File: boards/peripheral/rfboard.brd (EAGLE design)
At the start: 30 x 60 mm, 27 parts, among them Q1 IRLML5203, Q2 IRLML5203, Q3 IRLML5203, Q4 IRLML5203

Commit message: fixed improper ground issue
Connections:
- removed net N_GND: AMB2.2, C1.2, OPT101.3, OPT101.8
- net GND: now also AMB2.2, C1.2, OPT101.3, OPT101.8
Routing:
- removed copper zone on layer 16, net N_GND
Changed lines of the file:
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@@
 <via x="15.3162" y="55.2704" extent="1-16" drill="0.508" alwaysstop="yes"/>
 <wire x1="24.7904" y1="21.1582" x2="24.7904" y2="21.1836" width="0.6096" layer="16"/>
+<contactref element="AMB2" pad="2"/>
+<contactref element="C1" pad="2"/>
+<contactref element="OPT101" pad="8"/>
+<contactref element="OPT101" pad="3"/>
+<polygon width="0.6096" layer="16">
+<vertex x="30" y="19.5"/>
+<vertex x="30.1524" y="-0.1016"/>
+<vertex x="0.1524" y="-0.1016"/>
+<vertex x="0" y="19.5"/>
+</polygon>
 </signal>
 <signal name="AMB_OUT">
@@
 <wire x1="13.351" y1="26.7056" x2="13.351" y2="25.019" width="0.6096" layer="16"/>
 </signal>
-<signal name="N_GND" class="1">
-<contactref element="AMB2" pad="2"/>
-<contactref element="C1" pad="2"/>
-<contactref element="OPT101" pad="8"/>
-<contactref element="OPT101" pad="3"/>
-<polygon width="0.6096" layer="16">
-<vertex x="30" y="19.5"/>
-<vertex x="30.1524" y="-0.1016"/>
-<vertex x="0.1524" y="-0.1016"/>
-<vertex x="0" y="19.5"/>
-</polygon>
-</signal>
 <signal name="L4">

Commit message: Cleanup issues, working on powerboard res move
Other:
- board text added: "Xbee Forward"
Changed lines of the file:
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@@
 <?xml version="1.0" encoding="utf-8"?>
 <!DOCTYPE eagle SYSTEM "eagle.dtd">
-<eagle version="6.4">
+<eagle version="6.5.0">
 <drawing>
 <settings>
@@
 <setting verticaltext="up"/>
 </settings>
-<grid distance="1" unitdist="mil" unit="mil" style="lines" multiple="20" display="no" altdistance="0.025" altunitdist="inch" altunit="inch"/>
+<grid distance="0.02" unitdist="mm" unit="mm" style="lines" multiple="20" display="no" altdistance="0.025" altunitdist="inch" altunit="inch"/>
 <layers>
 <layer number="1" name="Top" color="4" fill="1" visible="yes" active="yes"/>
@@
 <text x="22.479" y="22.6314" size="0.8128" layer="25" rot="R90">AD4/DI4</text>
 <text x="2.7432" y="31.2928" size="0.8128" layer="25" rot="R90">8/6/13</text>
+<wire x1="24.0284" y1="42.799" x2="24.0284" y2="41.148" width="0.4064" layer="21"/>
+<wire x1="24.0284" y1="41.148" x2="27.178" y2="37.9984" width="0.4064" layer="21"/>
+<wire x1="27.178" y1="37.9984" x2="27.178" y2="26.2636" width="0.4064" layer="21"/>
+<wire x1="27.178" y1="26.2636" x2="23.7744" y2="22.86" width="0.4064" layer="21"/>
+<wire x1="23.7744" y1="22.86" x2="23.7744" y2="22.5044" width="0.4064" layer="21"/>
+<wire x1="23.7744" y1="22.5044" x2="23.6474" y2="22.3774" width="0.4064" layer="21"/>
+<text x="25.2222" y="37.1348" size="0.8128" layer="21" rot="R270">Xbee Forward</text>
+<wire x1="16.5862" y1="5.9436" x2="16.5354" y2="8.0264" width="0.4064" layer="21" curve="-180"/>
+<wire x1="16.5354" y1="8.0264" x2="16.5354" y2="9.779" width="0.4064" layer="21"/>
+<wire x1="16.5354" y1="5.8674" x2="16.5354" y2="4.064" width="0.4064" layer="21"/>
+<circle x="4" y="56" radius="3.668" width="0.4064" layer="21"/>
+<circle x="26" y="56" radius="3.668" width="0.4064" layer="21"/>
+<circle x="26" y="4" radius="3.668" width="0.4064" layer="21"/>
+<circle x="4" y="4" radius="3.668" width="0.4064" layer="21"/>
 </plain>
 <attributes>

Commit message: fixed PRF labels
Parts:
- AMB2: value 96k -> 200k
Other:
- board text added: "v.2013/09/26"
- board text removed: "8/6/13"
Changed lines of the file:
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@@
 <text x="20.3708" y="22.5298" size="0.8128" layer="25" rot="R90">CTS/DI7</text>
 <text x="22.479" y="22.6314" size="0.8128" layer="25" rot="R90">AD4/DI4</text>
-<text x="2.7432" y="31.2928" size="0.8128" layer="25" rot="R90">8/6/13</text>
+<text x="2.6832" y="28.7328" size="0.8128" layer="25" rot="R90">v.2013/09/26</text>
 <wire x1="24.0284" y1="42.799" x2="24.0284" y2="41.148" width="0.4064" layer="21"/>
 <wire x1="24.0284" y1="41.148" x2="27.178" y2="37.9984" width="0.4064" layer="21"/>
@@
 <attribute name="VALUE" x="1.1684" y="7.5438" size="0.8128" layer="28" rot="MR90"/>
 </element>
-<element name="AMB2" library="resistor" package="R0805" value="96k" x="21.1328" y="14.986" smashed="yes" rot="MR0">
+<element name="AMB2" library="resistor" package="R0805" value="200k" x="21.1328" y="14.986" smashed="yes" rot="MR0">
 <attribute name="VALUE" x="22.3012" y="16.0782" size="0.8128" layer="28" rot="MR0"/>
 </element>

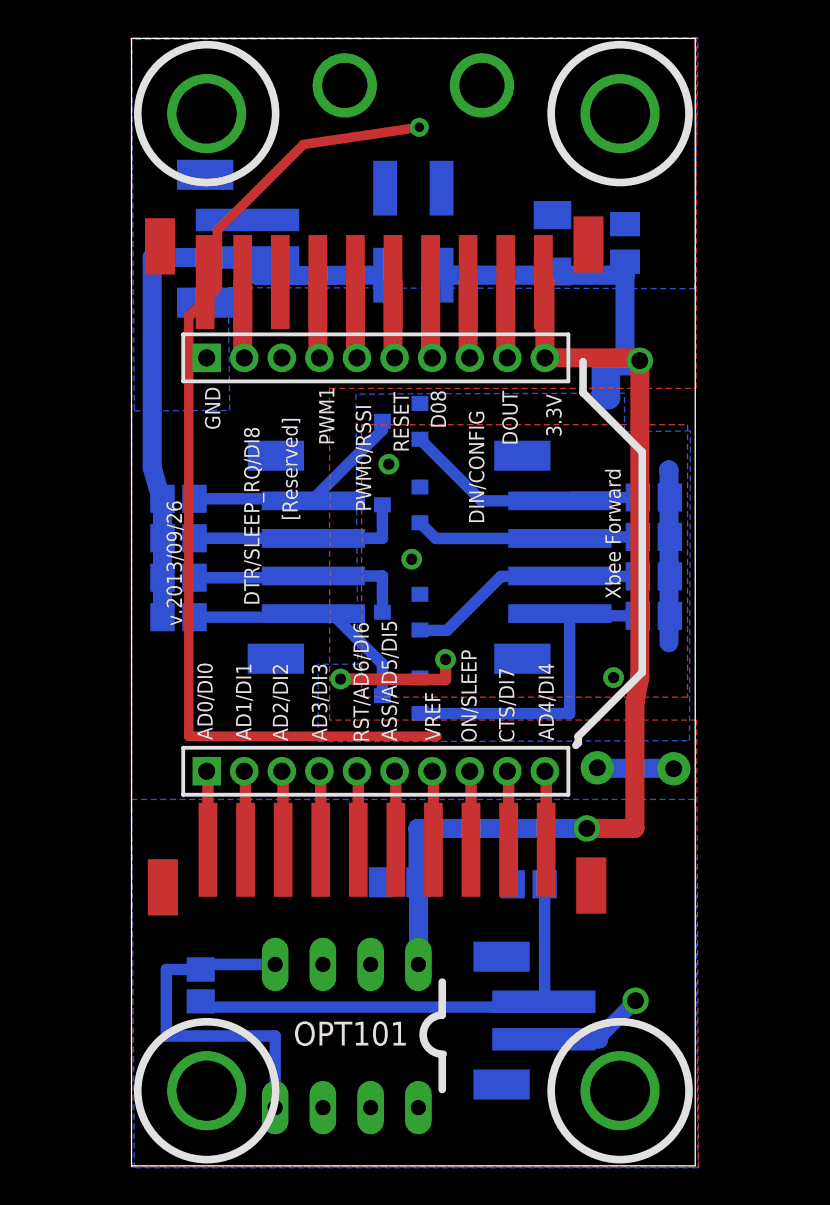
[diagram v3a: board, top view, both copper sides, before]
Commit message: changed size, moved holes, added servo header
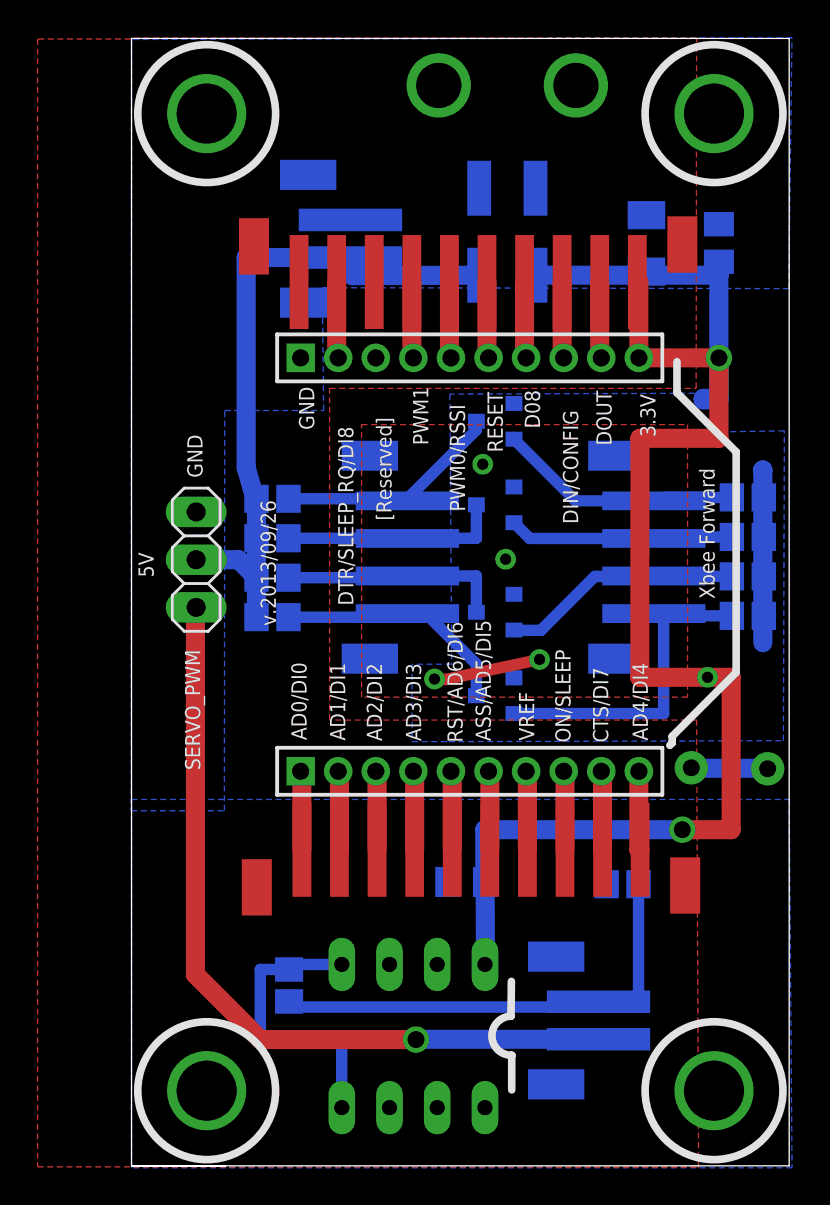
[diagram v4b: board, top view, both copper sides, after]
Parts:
- added JP3: (no value), pinhead:1X03
- moved LSM_PWR 5.48 mm to (6.90, 45.4)
- moved 3.3V 5.00 mm to (23.3, 26.4)
- moved AMB2 5.00 mm to (26.1, 15.0)
- moved C18 5.00 mm to (27.4, 49.1)
- moved C19 5.00 mm to (31.3, 49.1)
- moved JP1 5.00 mm to (18.0, 43.0)
- moved JP2 5.00 mm to (18.0, 21.0)
- moved R1 5.00 mm to (7.50, 35.5)
- moved R3 5.00 mm to (7.50, 31.3)
- moved R7 5.00 mm to (7.50, 29.2)
- moved R9 5.00 mm to (7.50, 33.4)
- moved U$1 5.00 mm to (6.09, 12.3)
- moved U$3 5.00 mm to (29.9, 51.5)
- moved X1 5.00 mm to (20.0, 57.5)
- moved 5V 5.00 mm to (10.2, 26.4)
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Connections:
- removed net AMB_ON: U$2.P$1
- new net SERVO: JP3.1, U$2.P$1
- net 5V: now also JP3.2
- net GND: now also JP3.3
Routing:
- net GND: track 58.1 -> 4.67 mm, vias 3 -> 2
- net SERVO: track 0.00 -> 44.6 mm, vias 0 -> 1
- net 3.3V: track 91.3 -> 97.3 mm
- net AMB_ON: track 5.81 -> 0.00 mm, vias 1 -> 0
- net 5V: track 32.2 -> 36.2 mm
- net AMB_LOW: track 25.1 -> 28.4 mm
- net AMB_OUT: track 19.2 -> 16.1 mm
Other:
- board size 30 x 60 mm -> 35 x 60 mm
- board text added: "5V"
- board text added: "SERVO_PWM"
